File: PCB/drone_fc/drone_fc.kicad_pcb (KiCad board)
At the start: 4 copper layers, 36 x 36 mm, 52 parts, among them J1 USB_C_Receptacle_USB2.0_16P, J2 Conn_ARM_SWD_TagConnect_TC2030, J3 Conn_01x04_Socket, J4 Conn_01x08_Socket, Q1 BSS138, Q3 BSS138BKS, SW1 PTS815SJM250SMTRLFS, U1 USBLC6-2SC6, U2 MCP1703AT-3302E/MB, U3 nRF52840, U4 LP5907MFX-1.8, U6 ICM-20948, X1 32MHz

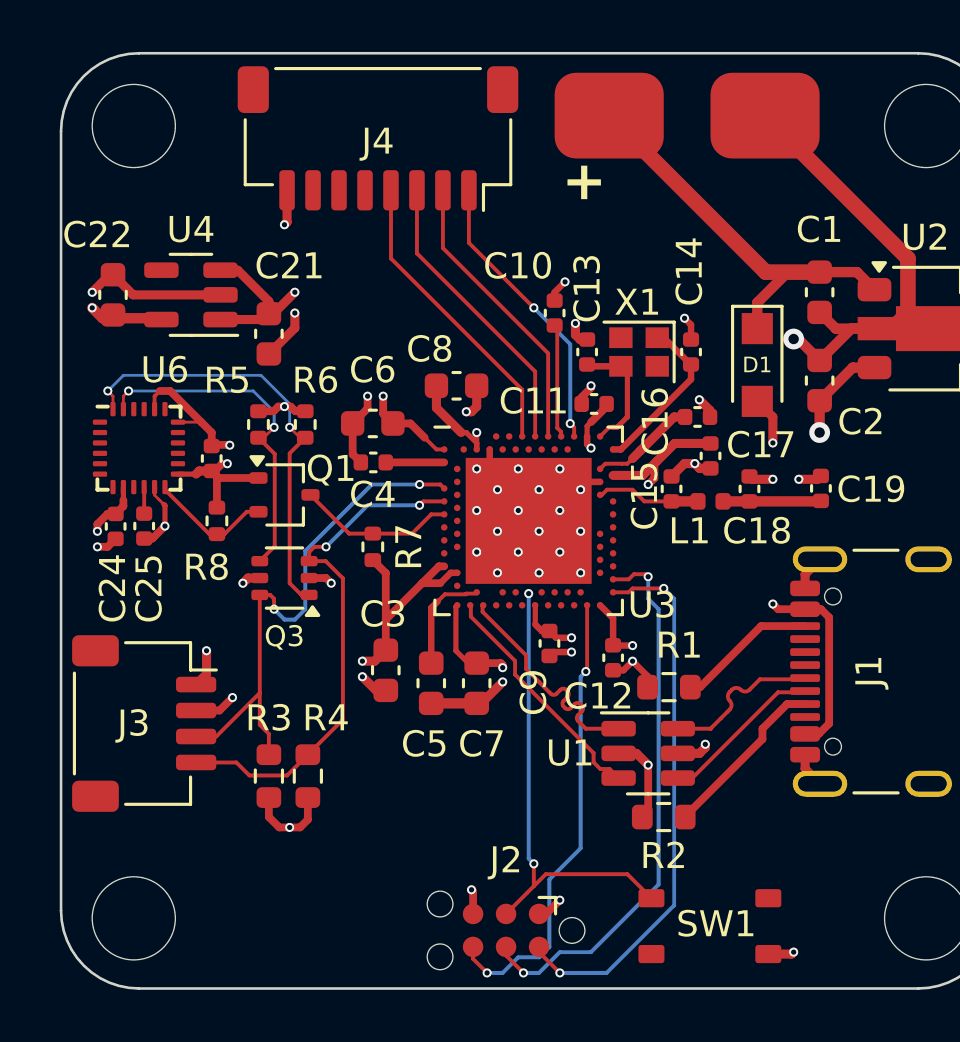
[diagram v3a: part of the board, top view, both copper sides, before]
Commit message: Made sure no traces were under vias and turned them into through holes because JLCPCB doesn't support blind vias and it's cheaper like this anyway
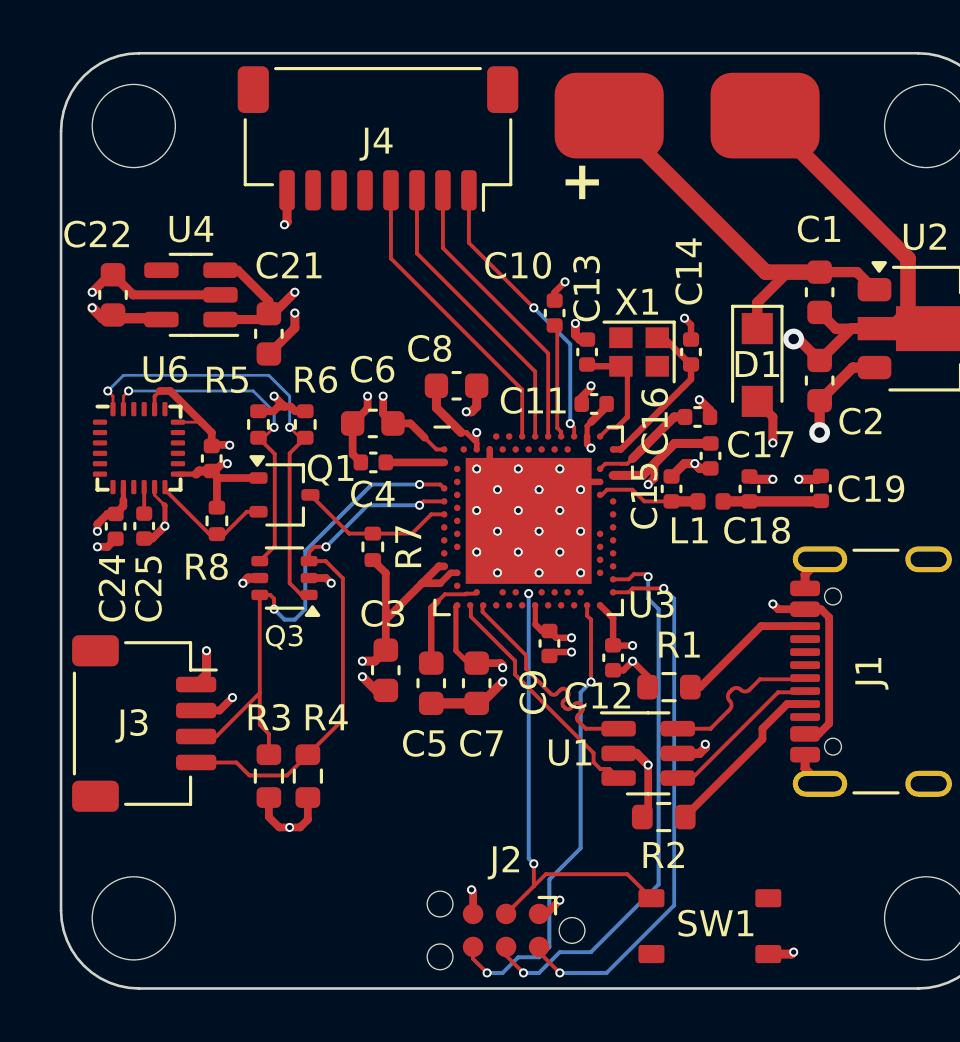
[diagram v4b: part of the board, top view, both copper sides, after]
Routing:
- net /DEC4_6: track 16.6 -> 17.5 mm
- net +1V8: track 13.6 -> 14.2 mm
